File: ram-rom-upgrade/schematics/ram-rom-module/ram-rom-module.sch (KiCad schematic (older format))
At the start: 16 parts, among them SW1 SW_DIP_x08, SW2 SW_Push, U1 74LS245, U2 UM61512A, U3 74LS157, U4 28C256, U5 74LS157, U6 74LS157, U7 74LS00, U8 74LS32

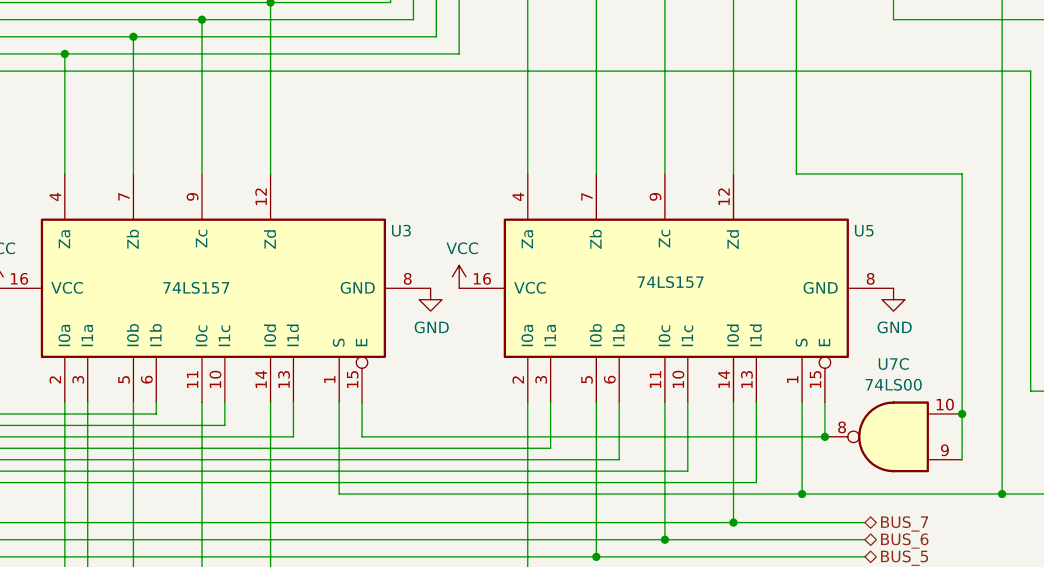
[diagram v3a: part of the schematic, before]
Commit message: corrected yet another bus contention
The 74LS157 that select the data bus or switches for the RAM in value were switch to 74LS257 models so that the output is high Z when the chip is not enabled.
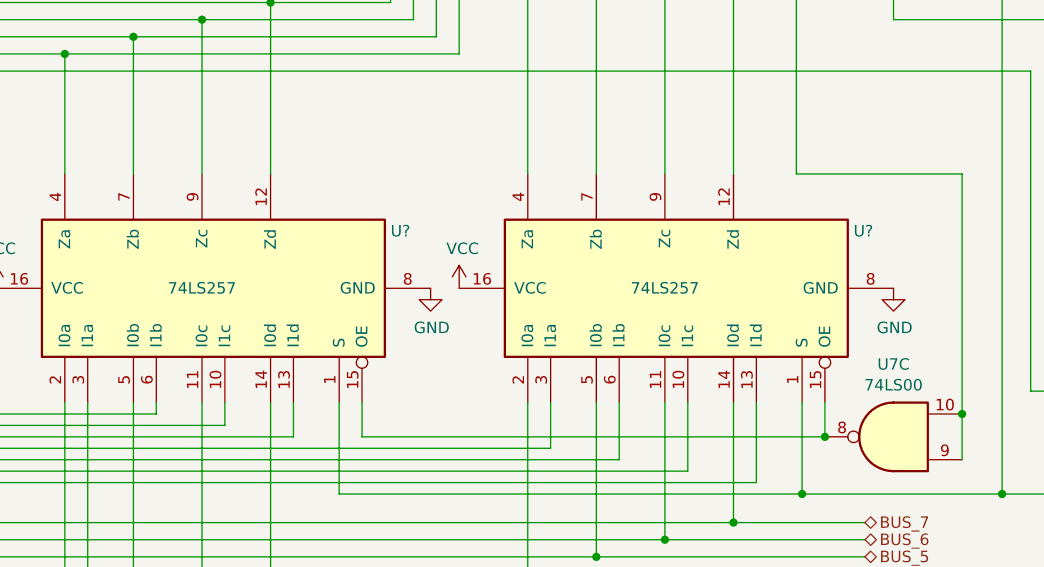
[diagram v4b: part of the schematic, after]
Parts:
- removed U3, U5: 74LS157, symbol 74xx:74LS157
- added U? (x2): 74LS257, symbol ram-rom-upgrade-symbols:74LS257
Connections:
- net BUS_0: now also U?.2 (I0a)
- net BUS_1: now also U?.5 (I0b)
- net BUS_2: now also U?.11 (I0c)
- net BUS_3: now also U?.14 (I0d)
- net BUS_4: now also U?.2 (I0a)
- net BUS_5: now also U?.5 (I0b)
- net BUS_6: now also U?.11 (I0c)
- net BUS_7: now also U?.14 (I0d)
- net GND: now also U?.8 (GND), U?.8 (GND)
- net PROG: now also U?.1 (S), U?.1 (S)
- net VCC: now also U?.16 (VCC), U?.16 (VCC)
- net at BAR1.1 (A), U1.2 (A0), U2.13 (I/O1)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: now also U?.4 (Za)
- net at BAR1.2 (A), U1.3 (A1), U2.14 (I/O2)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: now also U?.7 (Zb)
- net at BAR1.3 (A), U1.4 (A2), U2.15 (I/O3)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: now also U?.9 (Zc)
- net at BAR1.4 (A), U1.5 (A3), U2.17 (I/O4)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: now also U?.12 (Zd)
- net at BAR1.5 (A), U1.6 (A4), U2.18 (I/05)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: now also U?.4 (Za)
- net at BAR1.6 (A), U1.7 (A5), U2.19 (I/O6)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: now also U?.7 (Zb)
- net at BAR1.7 (A), U1.8 (A6), U2.20 (I/O7)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: now also U?.9 (Zc)
- net at BAR1.8 (A), U1.9 (A7), U2.21 (I/O8)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: now also U?.12 (Zd)
- net at SW1.3: now also U?.10 (I1c)
- net at SW1.4: now also U?.13 (I1d)
- net at U7.8: now also U?.15 (OE), U?.15 (OE)
- net at SW1.1: now also U?.3 (I1a)
- net at SW1.2: now also U?.6 (I1b)
- net at SW1.7: now also U?.10 (I1c)
- net at SW1.8: now also U?.13 (I1d)
- net at SW1.5: now also U?.3 (I1a)
- net at SW1.6: now also U?.6 (I1b)
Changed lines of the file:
@@
 Text HLabel 8150 5775 2    50   BiDi ~ 0
 BUS_7
-$Comp
-L 74xx:74LS157 U5
-U 1 1 60556B06
-P 7275 4750
-F 0 "U5" V 7525 3925 50  0000 R CNN
-F 1 "74LS157" V 7300 4875 50  0000 R CNN
-F 2 "" H 7275 4750 50  0001 C CNN
-F 3 "http://www.ti.com/lit/gpn/sn74LS157" H 7275 4750 50  0001 C CNN
-	1    7275 4750
-	0    -1   -1   0
-$EndComp
 Wire Wire Line
 	7575 3200 7575 4250
@@
 Wire Wire Line
 	5250 3575 5250 4250
-$Comp
-L 74xx:74LS157 U3
-U 1 1 6055348B
-P 5250 4750
-F 0 "U3" V 5500 3925 50  0000 R CNN
-F 1 "74LS157" V 5250 4925 50  0000 R CNN
-F 2 "" H 5250 4750 50  0001 C CNN
-F 3 "http://www.ti.com/lit/gpn/sn74LS157" H 5250 4750 50  0001 C CNN
-	1    5250 4750
-	0    -1   -1   0
-$EndComp
 Wire Wire Line
 	7875 5650 5850 5650
@@
 Wire Wire Line
 	8275 1375 8275 1825
+$Comp
+L ram-rom-upgrade-symbols:74LS257 U?
+U 1 1 607C5143
+P 7275 4750
+F 0 "U?" V 7525 3925 50  0000 R CNN
+F 1 "74LS257" V 7275 4900 50  0000 R CNN
+F 2 "" H 7275 4750 50  0001 C CNN
+F 3 "http://www.ti.com/lit/gpn/sn74LS257" H 7275 4750 50  0001 C CNN
+	1    7275 4750
+	0    -1   -1   0
+$EndComp
+$Comp
+L ram-rom-upgrade-symbols:74LS257 U?
+U 1 1 60814B6F
+P 5250 4750
+F 0 "U?" V 5500 3925 50  0000 R CNN
+F 1 "74LS257" V 5250 4900 50  0000 R CNN
+F 2 "" H 5250 4750 50  0001 C CNN
+F 3 "http://www.ti.com/lit/gpn/sn74LS257" H 5250 4750 50  0001 C CNN
+	1    5250 4750
+	0    -1   -1   0
+$EndComp
 $EndSCHEMATC

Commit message: minor modifications
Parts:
- R2: value 10K Ω -> 1K Ω
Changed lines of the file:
@@
 P 8975 3025
 F 0 "R2" V 9050 2975 50  0000 L CNN
-F 1 "10K Ω" V 8900 2925 50  0000 L CNN
+F 1 "1K Ω" V 8900 2925 50  0000 L CNN
 F 2 "" H 8975 3025 50  0001 C CNN
 F 3 "~" H 8975 3025 50  0001 C CNN

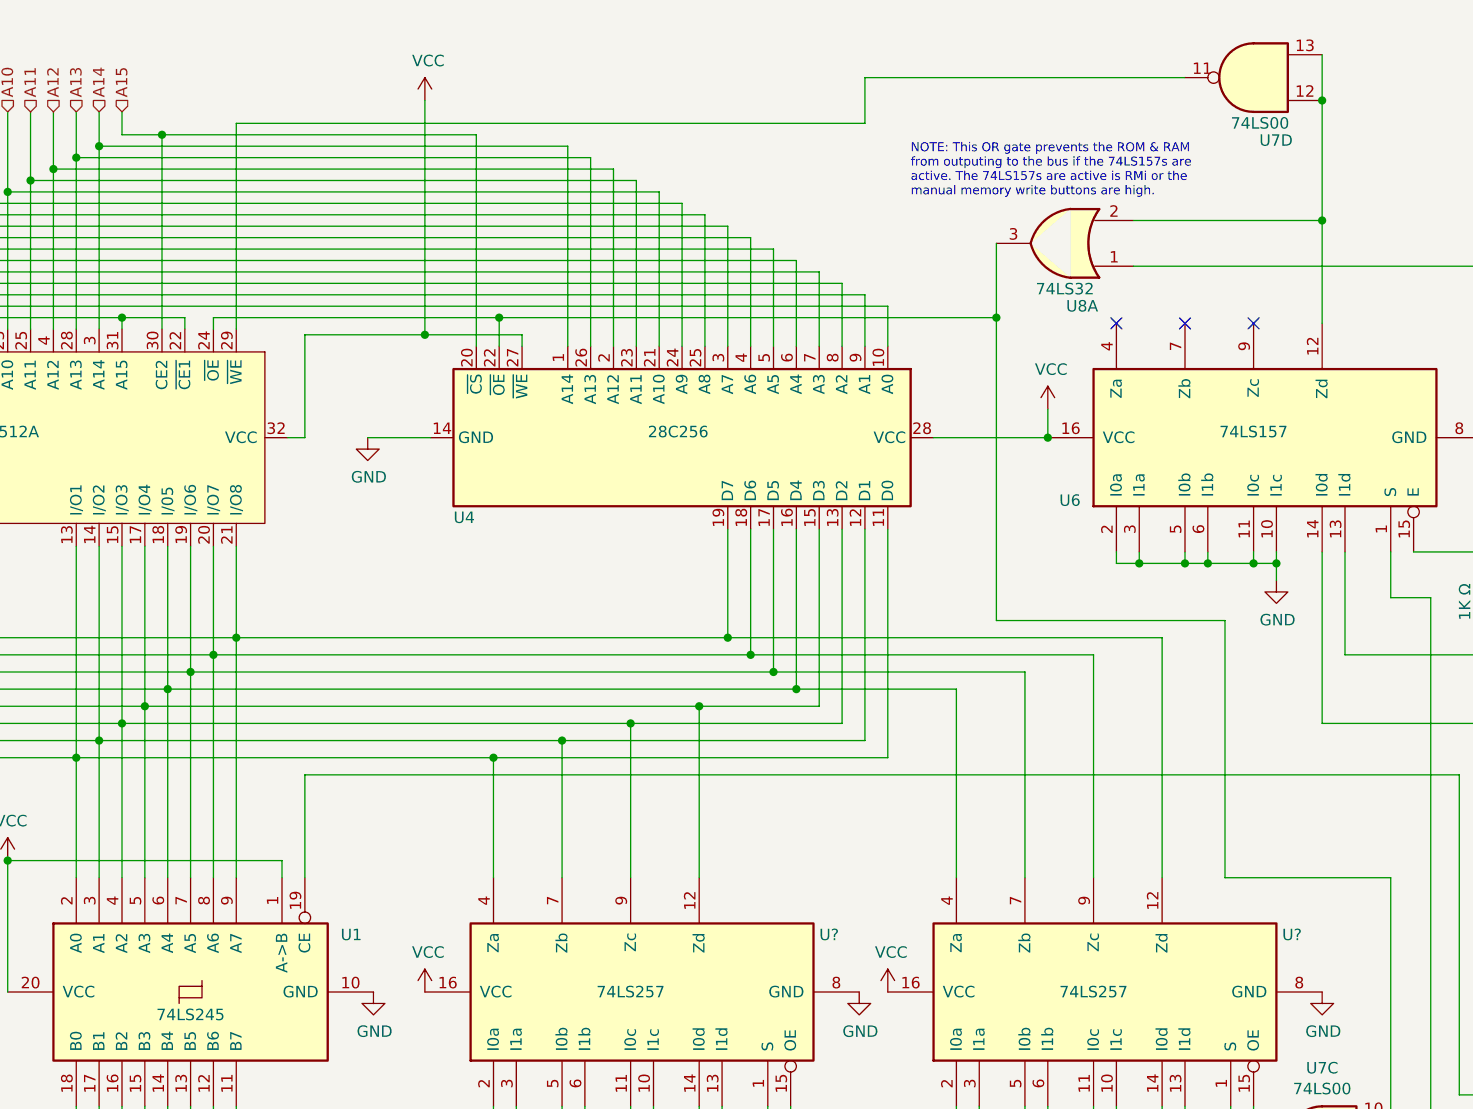
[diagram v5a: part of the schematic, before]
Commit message: fixed quasi-enable issue for UM61512A
Turns out that both of the YM61512A enable lines need to be in a disable state for the output lines to be fully put into a high impedance state.
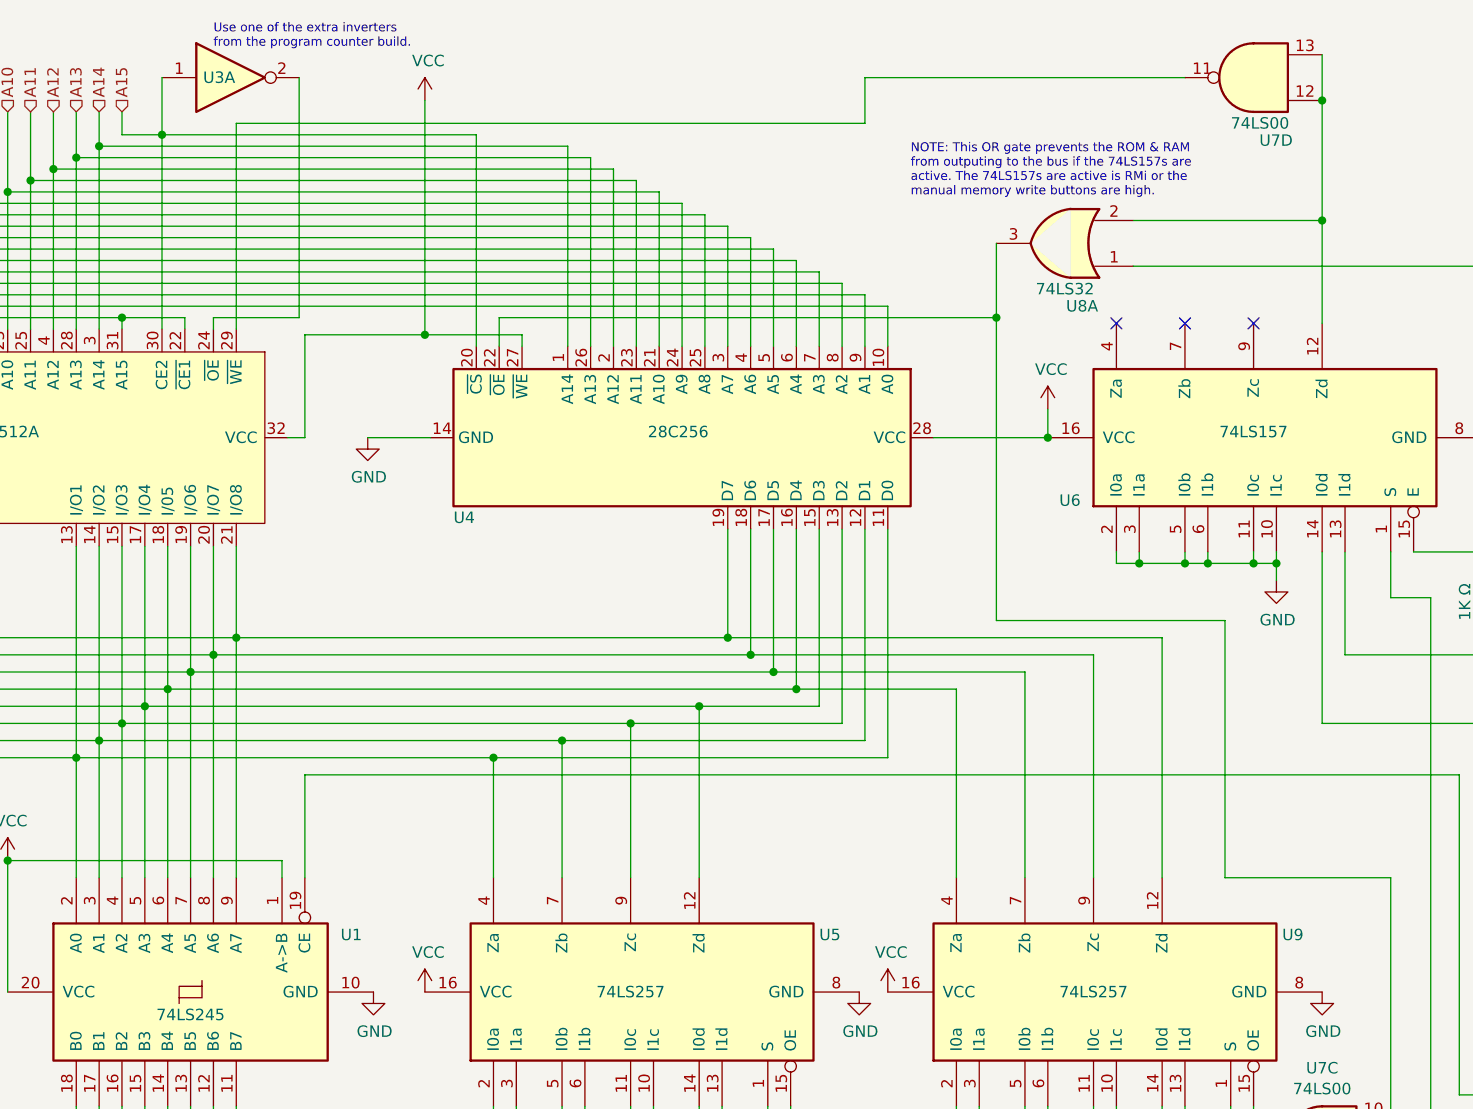
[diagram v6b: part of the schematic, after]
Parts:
- added U3: 74LS04, symbol 74xx:74LS04
- gave numbers to parts that had none: 2
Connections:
- net A15: now also U3.1
- net at U4.22 (~OE), U7.10, U7.9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: no longer U2.24 (~OE)
- new net: U2.24 (~OE), U3.2
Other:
- note added: "Use one of the extra inverters\nfrom the program counter build."
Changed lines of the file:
@@
 	4100 2325 4375 2325
-Wire Wire Line
-	3425 1850 3425 1800
 Wire Wire Line
 	5675 2725 5675 3200
@@
 	7575 3200 5675 3200
 Wire Wire Line
-	3425 1800 4675 1800
-Wire Wire Line
 	3200 1000 4575 1000
 Wire Wire Line
@@
 Wire Wire Line
 	4675 1800 6850 1800
-Connection ~ 4675 1800
 Wire Wire Line
 	8750 5650 10925 5650
@@
 	8275 1375 8275 1825
 $Comp
-L ram-rom-upgrade-symbols:74LS257 U?
+L ram-rom-upgrade-symbols:74LS257 U9
 U 1 1 607C5143
 P 7275 4750
-F 0 "U?" V 7525 3925 50  0000 R CNN
+F 0 "U9" V 7525 3925 50  0000 R CNN
 F 1 "74LS257" V 7275 4900 50  0000 R CNN
 F 2 "" H 7275 4750 50  0001 C CNN
@@
 $EndComp
 $Comp
-L ram-rom-upgrade-symbols:74LS257 U?
+L ram-rom-upgrade-symbols:74LS257 U5
 U 1 1 60814B6F
 P 5250 4750
-F 0 "U?" V 5500 3925 50  0000 R CNN
+F 0 "U5" V 5500 3925 50  0000 R CNN
 F 1 "74LS257" V 5250 4900 50  0000 R CNN
 F 2 "" H 5250 4750 50  0001 C CNN
@@
 	0    -1   -1   0
 $EndComp
+$Comp
+L 74xx:74LS04 U3
+U 1 1 60BA129D
+P 3500 750
+F 0 "U3" H 3450 750 50  0000 C CNN
+F 1 "74LS04" H 3500 976 50  0001 C CNN
+F 2 "" H 3500 750 50  0001 C CNN
+F 3 "http://www.ti.com/lit/gpn/sn74LS04" H 3500 750 50  0001 C CNN
+	1    3500 750
+	1    0    0    -1
+$EndComp
+Wire Wire Line
+	3200 1000 3200 750
+Wire Wire Line
+	3800 750  3800 1800
+Wire Wire Line
+	3800 1800 3425 1800
+Wire Wire Line
+	3425 1800 3425 1850
+Text Notes 3425 625  0    39   ~ 0
+Use one of the extra inverters\nfrom the program counter build.
 $EndSCHEMATC
